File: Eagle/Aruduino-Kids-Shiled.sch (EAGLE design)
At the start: 16 parts

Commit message: Second
few changes
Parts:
- added U$3: SIPS-7, Aruduino-Kids-Shiled:SIPS-7
- U$6: value C-03784 -> SIPS-2; device Aruduino-Kids-Shiled:C-03784 -> Aruduino-Kids-Shiled:SIPS-2
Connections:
- new net N$25: U$1.P$13, U$3.P$7
- new net N$26: U$1.P$16, U$6.P$1
- new net N$27: U$1.P$15, U$6.P$2
- net N$10: now also U$3.P$1; no longer U$6.P$1
- net N$12: now also U$3.P$4; no longer U$6.P$6
- net N$14: now also U$3.P$2; no longer U$6.P$2
- net N$15: now also U$3.P$3; no longer U$6.P$3
- net N$16: now also U$1.P$5, U$3.P$5; no longer U$1.P$4, U$6.P$4
- net N$17: now also U$1.P$4, U$3.P$6; no longer U$1.P$5, U$6.P$5

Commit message: Semi_Final
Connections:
- removed net N$1: LED1.A, LED2.A, T-SW1.2COM, TACTSW1.1, TACTSW1.3, TACTSW2.1, TACTSW2.3, TB1.P$2, TB2.P$2, U$1.P$22, U$4.S, U$5.S
- removed net N$19: U$1.P$18, U$4.G
- removed net N$2: LED1.C, U$1.P$14
- removed net N$20: U$1.P$24, U$5.G
- removed net N$3: LED2.C, U$1.P$28
- new net GND: LED1.A, LED2.A, T-SW1.2COM, TACTSW1.1, TACTSW1.3, TACTSW2.1, TACTSW2.3, TB1.P$2, TB2.P$2, U$1.22, U$4.S, U$5.S
- new net P14: LED1.C, U$1.14
- new net P18: U$1.18, U$4.G
- new net P24: U$1.24, U$5.G
- new net P28: LED2.C, U$1.28
- net N$10: now also U$1.1, U$3.1; no longer U$1.P$1, U$3.P$1
- net N$11: now also U$1.23; no longer U$1.P$23
- net N$12: now also U$1.27, U$3.4; no longer U$1.P$27, U$3.P$4
- net N$13: now also U$1.25; no longer U$1.P$25
- net N$14: now also U$1.2, U$3.2; no longer U$1.P$2, U$3.P$2
- net N$15: now also U$1.6, U$3.3; no longer U$1.P$6, U$3.P$3
- net N$16: now also U$1.5, U$3.5; no longer U$1.P$5, U$3.P$5
- net N$17: now also U$1.4, U$3.6; no longer U$1.P$4, U$3.P$6
- net N$18: now also U$1.26; no longer U$1.P$26
- net N$25: now also U$1.13, U$3.7; no longer U$1.P$13, U$3.P$7
- net N$26: now also U$1.16; no longer U$1.P$16
- net N$27: now also U$1.15; no longer U$1.P$15
- net N$4: now also U$1.10; no longer U$1.P$10
- net N$5: now also U$1.11; no longer U$1.P$11
- net N$6: now also U$1.7; no longer U$1.P$7
- net N$7: now also U$1.8; no longer U$1.P$8
- net N$8: now also U$1.9; no longer U$1.P$9
- net N$9: now also U$1.17; no longer U$1.P$17
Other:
- moved on the sheet: 0-50C, C1, LED1, LED2, R1, T-SW1, TACTSW1, TACTSW2, U$2, U$4, U$5, VR.1

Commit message: Practice-Final
Test-Build
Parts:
- added R2: 1K, Aruduino-Kids-Shiled:R
- added U$10, U$9: SIPS-2, Aruduino-Kids-Shiled:SIPS-2
- R1: value 100K -> 10K
- TACTSW1, TACTSW2: value SW -> (none)
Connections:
- removed net N$7: U$1.8, VR.1.A
- new net N$33: 0-50C.2, R2.2, U$1.10
- net GND: now also LED1.C, LED2.C, TACTSW1.2, TACTSW1.4, TACTSW2.2, TACTSW2.4, U$10.P$2, U$9.P$2; no longer LED1.A, LED2.A, TACTSW1.1, TACTSW1.3, TACTSW2.1, TACTSW2.3
- net N$11: now also TACTSW2.1, TACTSW2.3; no longer TACTSW2.2, TACTSW2.4
- net N$4: now also R2.1, U$1.7, U$2.C, VR.1.E; no longer 0-50C.2, U$1.10
- net N$5: now also R1.1; no longer R1.2
- net N$6: now also R1.2, U$1.8, VR.1.A; no longer R1.1, U$1.7, U$2.C, VR.1.E
- net N$8: now also U$3.8
- net N$9: now also TACTSW1.1, TACTSW1.3; no longer TACTSW1.2, TACTSW1.4
- net P14: now also LED1.A; no longer LED1.C
- net P18: now also U$10.P$1
- net P24: now also U$9.P$1
- net P28: now also LED2.A; no longer LED2.C
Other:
- note added: "JP1"
- note added: "JP2"
- note added: "JP3"
- note added: "JP4"
- note added: "Tr1"
- note added: "Tr2"
- note added: "dp1-(miso-SPI)-PwmOut"
- note added: "dp13-(AnalogIn)"
- note added: "dp15(Serial-RX)"
- note added: "dp16(Serial-TX)"
- note added: "dp2-(mosi-SPI)-PwmOut"
- note added: "dp27(SCl-I2C)"
- note added: "dp4-(AnalogIn)"
- note added: "dp5-(sda-I2C)"
- note added: "dp6(sck-SPI)"
- note added: "dp8-(AnalogGND)"
- note added: "mbed 1114FN28"
- moved on the sheet: C1, LED1, LED2, R1, T-SW1, VR.1

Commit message: Final-P-ban
1st time
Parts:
- R2: value 1K -> 7.5K
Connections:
- net GND renamed N$126
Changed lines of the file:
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@@
 <part name="SUPPLY12" library="supply2" deviceset="V&lt;--" device="" value="P18"/>
 <part name="SUPPLY13" library="supply2" deviceset="GND" device=""/>
-<part name="R2" library="Aruduino-Kids-Shiled" deviceset="R" device="" value="1K"/>
+<part name="R2" library="Aruduino-Kids-Shiled" deviceset="R" device="" value="7.5K"/>
 <part name="TACTSW2" library="Aruduino-Kids-Shiled" deviceset="TACT-SW" device=""/>
 <part name="TACTSW1" library="Aruduino-Kids-Shiled" deviceset="TACT-SW" device=""/>
@@
 </segment>
 <segment>
-<wire x1="203.2" y1="71.755" x2="200.025" y2="71.755" width="0.1524" layer="91"/>
 <pinref part="LED1" gate="G$1" pin="A"/>
 <wire x1="200.025" y1="71.755" x2="189.865" y2="71.755" width="0.1524" layer="91"/>
-<junction x="200.025" y="71.755"/>
 </segment>
 </net>
@@
 </segment>
 <segment>
-<wire x1="203.2" y1="61.595" x2="200.025" y2="61.595" width="0.1524" layer="91"/>
 <pinref part="LED2" gate="G$1" pin="A"/>
 <wire x1="200.025" y1="61.595" x2="189.865" y2="61.595" width="0.1524" layer="91"/>
-<junction x="200.025" y="61.595"/>
 </segment>
 </net>
@@
 <wire x1="98.425" y1="-20.955" x2="98.425" y2="-27.94" width="0.1524" layer="91"/>
 <junction x="98.425" y="-20.955"/>
-<wire x1="92.075" y1="-27.94" x2="94.615" y2="-27.94" width="0.1524" layer="91"/>
 <pinref part="C1" gate="G$1" pin="1"/>
 <wire x1="94.615" y1="-27.94" x2="98.425" y2="-27.94" width="0.1524" layer="91"/>
-<junction x="94.615" y="-27.94"/>
 <wire x1="91.44" y1="-4.445" x2="92.075" y2="-4.445" width="0.1524" layer="91"/>
 <wire x1="92.075" y1="-4.445" x2="98.425" y2="-4.445" width="0.1524" layer="91"/>
@@
 </segment>
 </net>
-<net name="GND" class="0">
+<net name="N$126" class="0">
 <segment>
 <pinref part="SUPPLY3" gate="GND" pin="GND"/>
@@
 </segment>
 <segment>
-<wire x1="286.385" y1="45.085" x2="286.385" y2="56.515" width="0.1524" layer="91"/>
+<wire x1="286.385" y1="45.085" x2="286.385" y2="61.595" width="0.1524" layer="91"/>
 <pinref part="SUPPLY9" gate="GND" pin="GND"/>
 <wire x1="286.385" y1="61.595" x2="286.385" y2="71.755" width="0.1524" layer="91"/>
-<wire x1="205.105" y1="71.755" x2="207.645" y2="71.755" width="0.1524" layer="91"/>
 <wire x1="207.645" y1="71.755" x2="286.385" y2="71.755" width="0.1524" layer="91"/>
-<wire x1="205.74" y1="61.595" x2="207.645" y2="61.595" width="0.1524" layer="91"/>
+<pinref part="LED1" gate="G$1" pin="C"/>
+<pinref part="LED2" gate="G$1" pin="C"/>
 <wire x1="207.645" y1="61.595" x2="286.385" y2="61.595" width="0.1524" layer="91"/>
-<wire x1="286.385" y1="61.595" x2="286.385" y2="56.515" width="0.1524" layer="91"/>
-<pinref part="LED1" gate="G$1" pin="C"/>
-<junction x="207.645" y="71.755"/>
-<pinref part="LED2" gate="G$1" pin="C"/>
-<junction x="207.645" y="61.595"/>
 </segment>
 <segment>
@@
 <wire x1="184.15" y1="-54.61" x2="184.15" y2="-57.15" width="0.1524" layer="91"/>
 <pinref part="SUPPLY10" gate="GND" pin="GND"/>
-<junction x="184.15" y="-57.15"/>
 <pinref part="U$9" gate="G$1" pin="P$2"/>
 </segment>
@@
 <wire x1="183.642" y1="-42.164" x2="183.642" y2="-43.434" width="0.1524" layer="91"/>
 <pinref part="SUPPLY13" gate="GND" pin="GND"/>
-<wire x1="183.642" y1="-43.434" x2="183.642" y2="-45.339" width="0.1524" layer="91"/>
-<junction x="183.642" y="-43.434"/>
 </segment>
 </net>
@@
 <wire x1="221.615" y1="-27.305" x2="217.17" y2="-27.305" width="0.1524" layer="91"/>
 <pinref part="U$5" gate="G$1" pin="G"/>
-<junction x="221.615" y="-31.115"/>
 </segment>
 <segment>
@@
 <wire x1="81.915" y1="-36.83" x2="81.915" y2="-33.655" width="0.1524" layer="91"/>
 <junction x="81.915" y="-33.655"/>
-<wire x1="88.265" y1="-27.94" x2="86.995" y2="-27.94" width="0.1524" layer="91"/>
 <pinref part="C1" gate="G$1" pin="2"/>
 <wire x1="86.995" y1="-27.94" x2="85.09" y2="-27.94" width="0.1524" layer="91"/>
-<junction x="86.995" y="-27.94"/>
 <pinref part="U$1" gate="G$1" pin="11"/>
 </segment>
@@
 </sheet>
 </sheets>
+<errors>
+</errors>
 </schematic>
 </drawing>

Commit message: Test-Sample-Build
Jet-PCB
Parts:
- LED1: value 5V-12mA-Include-R -> I-06245-R
- LED2: value 5V-12mA-Include-R -> I-06245-G
- T-SW1: value SW -> P-00300
- TACTSW1: value (none) -> P-03646-B
- TACTSW2: value (none) -> P-03646-R
- TB1, TB2: value 2A -> P-01306
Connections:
- net N$4 renamed 3.3V
- removed net N$126: LED1.C, LED2.C, T-SW1.2COM, TACTSW1.2, TACTSW1.4, TACTSW2.2, TACTSW2.4, TB1.P$2, TB2.P$2, U$1.22, U$10.P$2, U$4.S, U$5.S, U$9.P$2
- removed net N$6: 0-50C.1, C1.1, R1.2, U$1.8, VR.1.A
- new net A-GND: 0-50C.1, C1.1, R1.2, U$1.8, U$3.8, VR.1.A
- new net GND: LED1.C, LED2.C, T-SW1.2COM, TACTSW1.2, TACTSW1.4, TACTSW2.2, TACTSW2.4, TB1.P2, TB2.P2, U$1.22, U$10.P2, U$4.S, U$5.S, U$9.P2
- net N$21: now also TB2.P1; no longer TB2.P$1
- net N$22: now also TB1.P1; no longer TB1.P$1
- net N$26: now also U$6.P1; no longer U$6.P$1
- net N$27: now also U$6.P2; no longer U$6.P$2
- net N$8: no longer U$3.8
- net P18: now also U$10.P1; no longer U$10.P$1
- net P24: now also U$9.P1; no longer U$9.P$1
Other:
- note added: "C-03785"
- note added: "C-05779 (TP2,TP3,TP4)"
- note added: "I-02426"
- note added: "P-01306"
- note added: "P-06113"
- note added: "P-06165"
- note added: "P-07258"
- note added: "P1"
- note added: "P2"
- note added: "R-25103"
- note added: "R-25752"
- note added: "TP1"
- note added: "TP2"
- note added: "TP3"
- note added: "TP4"
- note removed: "JP1"
- note removed: "JP2"
- note removed: "JP3"
- note removed: "JP4"
- moved on the sheet: C1, LED1, LED2, R1, R2, T-SW1, TACTSW1, TACTSW2, VR.1

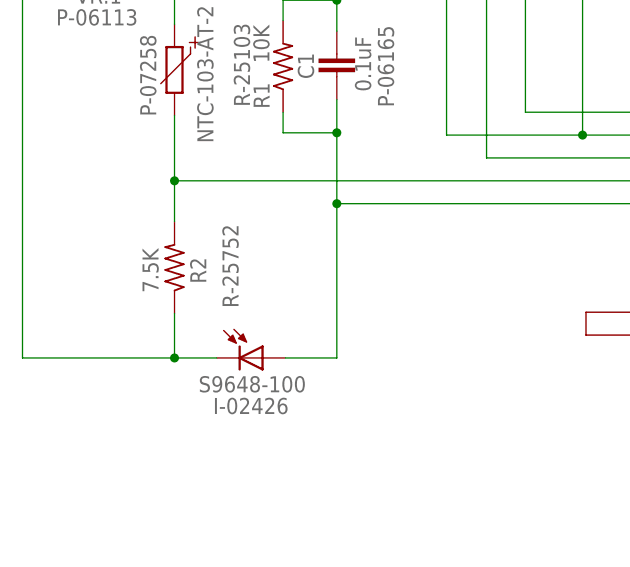
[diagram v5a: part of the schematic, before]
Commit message: Add dimensions
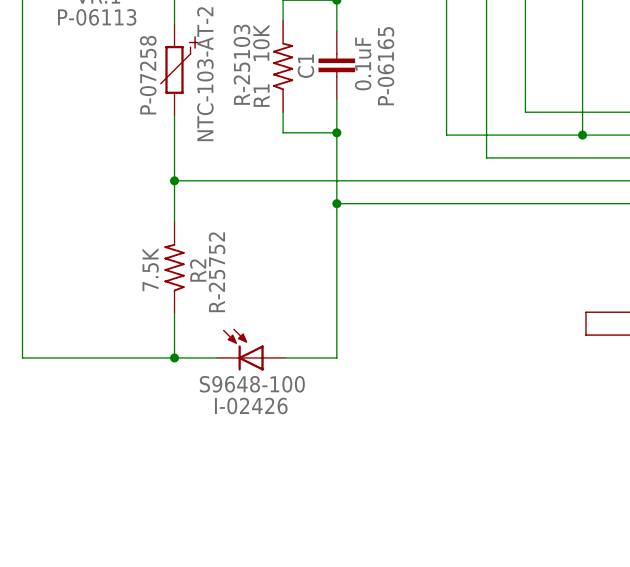
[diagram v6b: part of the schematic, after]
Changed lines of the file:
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@@
 <setting verticaltext="up"/>
 </settings>
-<grid distance="10" unitdist="mil" unit="mil" style="lines" multiple="1" display="no" altdistance="0.01" altunitdist="inch" altunit="inch"/>
+<grid distance="1" unitdist="mil" unit="mil" style="lines" multiple="1" display="no" altdistance="0.01" altunitdist="inch" altunit="inch"/>
 <layers>
 <layer number="1" name="Top" color="4" fill="1" visible="no" active="no"/>
@@
 <text x="-74.422" y="18.669" size="1.778" layer="95" rot="R90" align="bottom-right">R-25103</text>
 <text x="-58.42" y="18.415" size="1.778" layer="95" rot="R90" align="bottom-right">P-06165</text>
-<text x="-75.692" y="-3.683" size="1.778" layer="95" rot="R90" align="bottom-right">R-25752</text>
+<text x="-77.1906" y="-4.3688" size="1.778" layer="95" rot="R90" align="bottom-right">R-25752</text>
 <text x="-70.104" y="-24.765" size="1.778" layer="95" align="bottom-right">I-02426</text>
 <text x="27.178" y="-33.655" size="1.778" layer="95" align="bottom-right">C-05779
